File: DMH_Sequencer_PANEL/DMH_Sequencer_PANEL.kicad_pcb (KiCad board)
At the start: 2 copper layers, 300 x 200 mm, 107 parts, among them J0 Panel_GND_Solder_Wire_Pad

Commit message: Added range selection switch
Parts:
- H80: value Mode -> Range
- H82: value Quant -> 8 / 16
- moved H85 14.0 mm to (80.0, 145.0)
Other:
- board text added: "-5/+5"
- board text added: "0/+2"
- board text added: "0/+5"
- board text added: "Qnt"
- board text removed: "1x16"
- board text removed: "2x8"

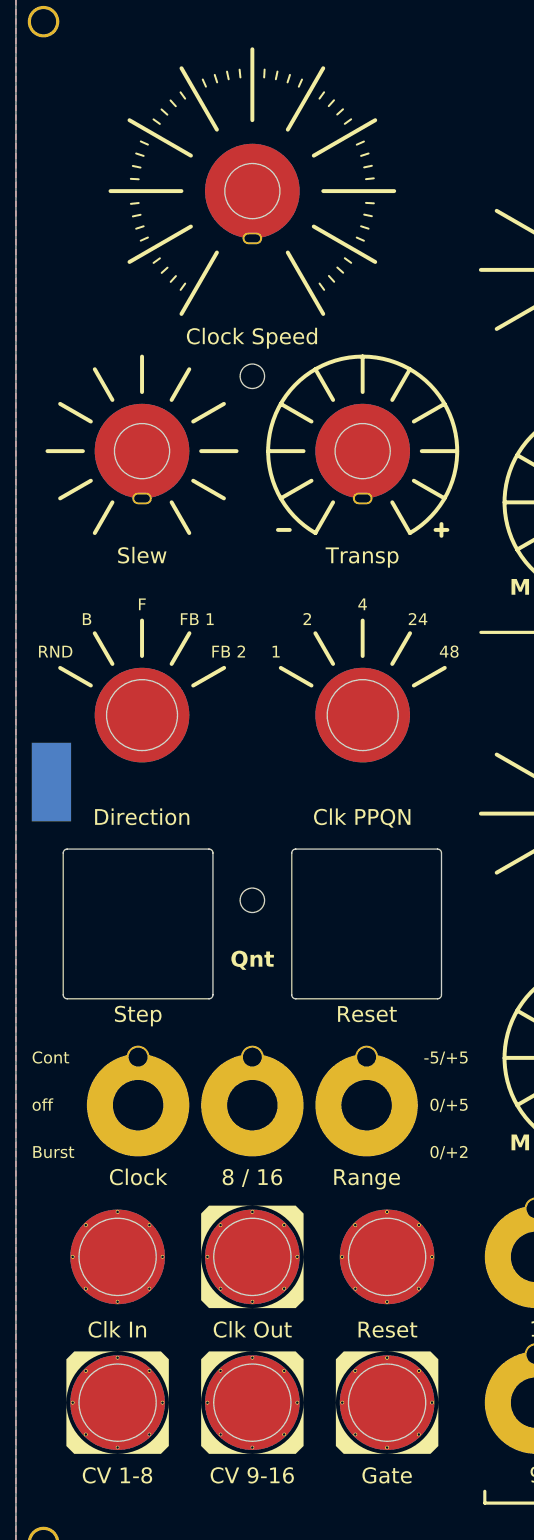
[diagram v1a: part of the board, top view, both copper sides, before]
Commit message: Added Gate out and Reset in for 9 to 16
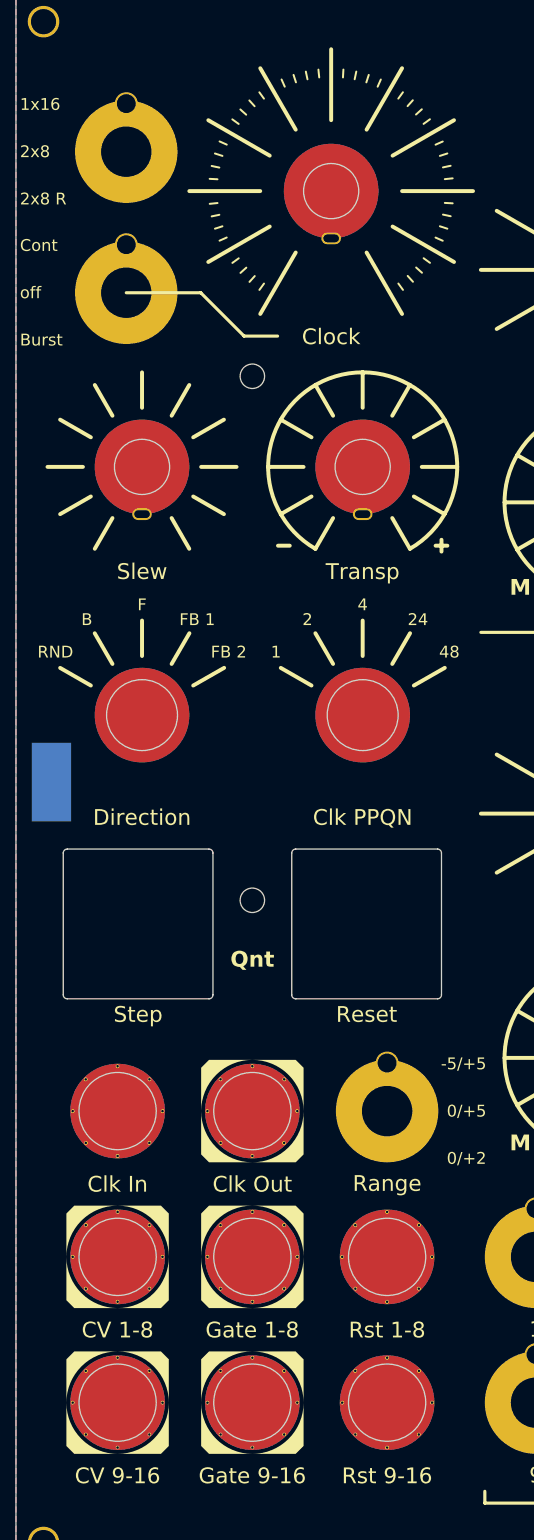
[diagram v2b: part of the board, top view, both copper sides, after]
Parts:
- added H116: Rst 1-8, SynthStuff:Jack_6.35mm_Cutout_v3, F.Cu at (97.1, 190.2)
- added H89: Gate 9-16, SynthStuff:Jack_6.35mm_Cutout_Output_v6, F.Cu at (80.0, 208.8)
- H73: value Clock Speed -> Clock
- H88: value Gate -> Gate 1-8
- H91: value Reset -> Rst 9-16
- moved H82 122.1 mm to (64.0, 50.0)
- moved H81 103.1 mm to (64.0, 67.9)
- moved H88 25.2 mm to (80.0, 190.2)
- moved H86 18.5 mm to (62.9, 190.2)
- moved H90 18.5 mm to (62.9, 171.8)
- moved H91 18.5 mm to (97.1, 208.8)
- moved H97 18.5 mm to (80.0, 171.8)
- moved H87 17.1 mm to (62.9, 208.8)
- moved H73 10.0 mm to (90.0, 55.0)
- moved H80 2.71 mm to (97.1, 171.8)
- moved H75 2.00 mm to (94.0, 90.0)
- moved H77 2.00 mm to (66.0, 90.0)
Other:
- board text added: "1x16"
- board text added: "2x8"
- board text added: "2x8 R"
